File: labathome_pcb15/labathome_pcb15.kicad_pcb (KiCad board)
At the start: 2 copper layers, 100 x 100 mm, 244 parts, among them J1 HALL, J10 BMEx80, J11 QWIIC, J12 TCS34725, J13 POWER, J14 AUX OUT, J15 CAN RS 485, J16 Headphones, J17 Micro_SD_Card_Det1, J18 K1, J19 BH1750, J2 I2C, J20 CCS811, J21 GPIO, J22 Volts, J23 VL53L5x, J24 K1, J26 STDC14, J27 ADDA, J28 Brushless, J3 AUX IN, J30 Srv4, J31 Srv1, J32 Srv2, J33 Srv3, J34 STM32 EXT, J4 SCD4x, J5 USB_ESP32, J6 PROG, J7 FAN5V, J8 3V GN RGB 5V, J9 Barrel_Jack_Switch, K1 G6K-2, M1 W5500_mini, Q1 BC817, Q2 IRLML6344, Q3 TIP41, Q4 BC817, Q5 IRLML6344, SW1 Reset, SW2 ON RS TERM, SW3 ON CAN TERM, SW4 BATT POWER, SW5 POWER, SW6 YELLOW, SW7 RED, SW8 GREEN, SW9 PROG 5V POWER, U1 MAX3485, U10 NAU8822, U11 AMS1117, U12 AHT20, U13 DS18B20, U14 BMP280, U15 NRF24L01, U16 LM358, U17 DS18B20, U2 IP5306, U21 IPS_240_240, U22 AM612, U24 SRV05, U27 TPS54202DDC, U3 DRV8313, U4 ESP32-S3-WROOM-1, U5 STM32G431R8Tx, U6 RFM95W-868S2, U7 SN65HVD230, U8 SRV05-4, U9 LSM6DS3, X1 FAN_6024, X3 SIM7080G

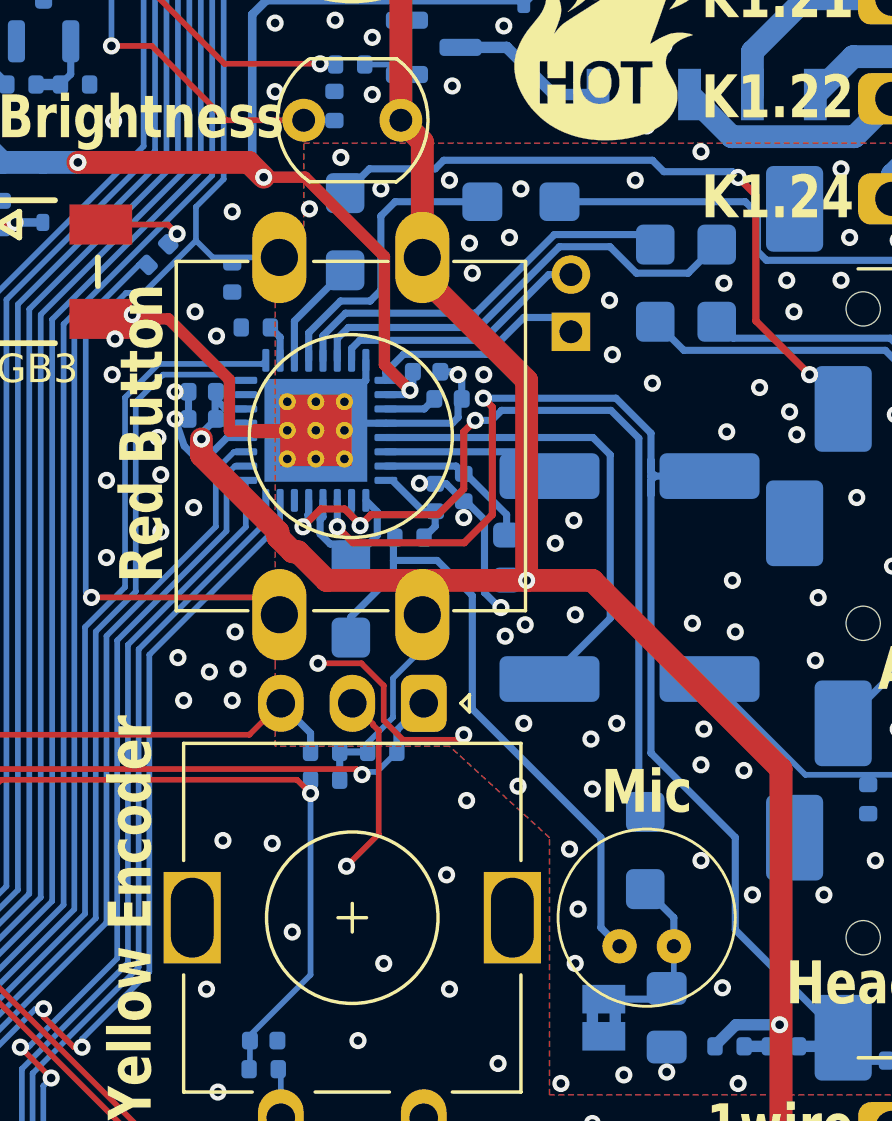
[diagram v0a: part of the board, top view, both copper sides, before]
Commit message: Added stm32 arduino firmware
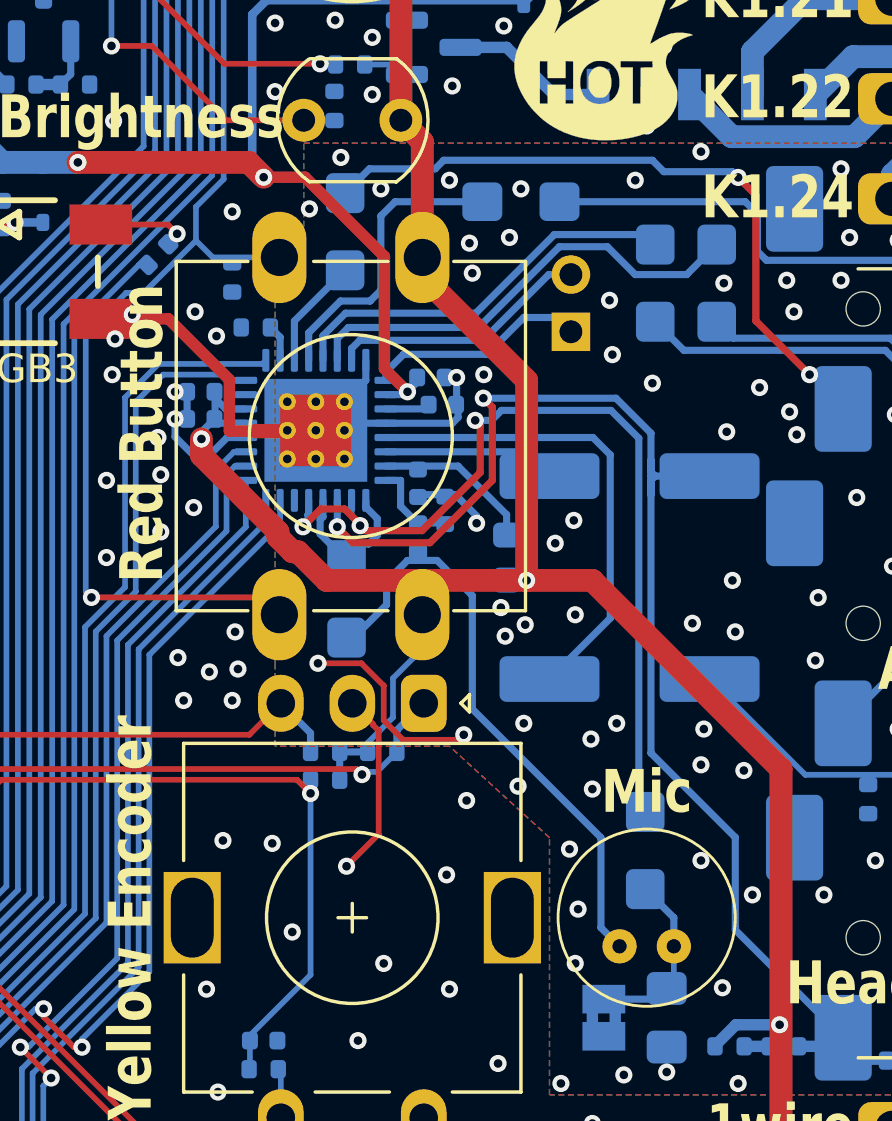
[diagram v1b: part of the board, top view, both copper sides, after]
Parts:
- moved C14 1.61 mm to (175.4, 99.1)
- moved C22 0.57 mm to (176.3, 100.0)
- moved R24 0.30 mm to (175.4, 101.0), turned to -90 degrees
- moved C21 0.28 mm to (176.2, 96.3)
- moved C15 0.25 mm to (175.8, 95.4)
- moved C23 0.15 mm to (172.9, 103.2)
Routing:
- net GNDA: track 22.1 -> 18.2 mm, vias 97 -> 96
- net Net-(MK1-+): track 21.7 -> 20.9 mm
- net /audioamplifier/JACK_DETECT: track 46.9 -> 46.2 mm

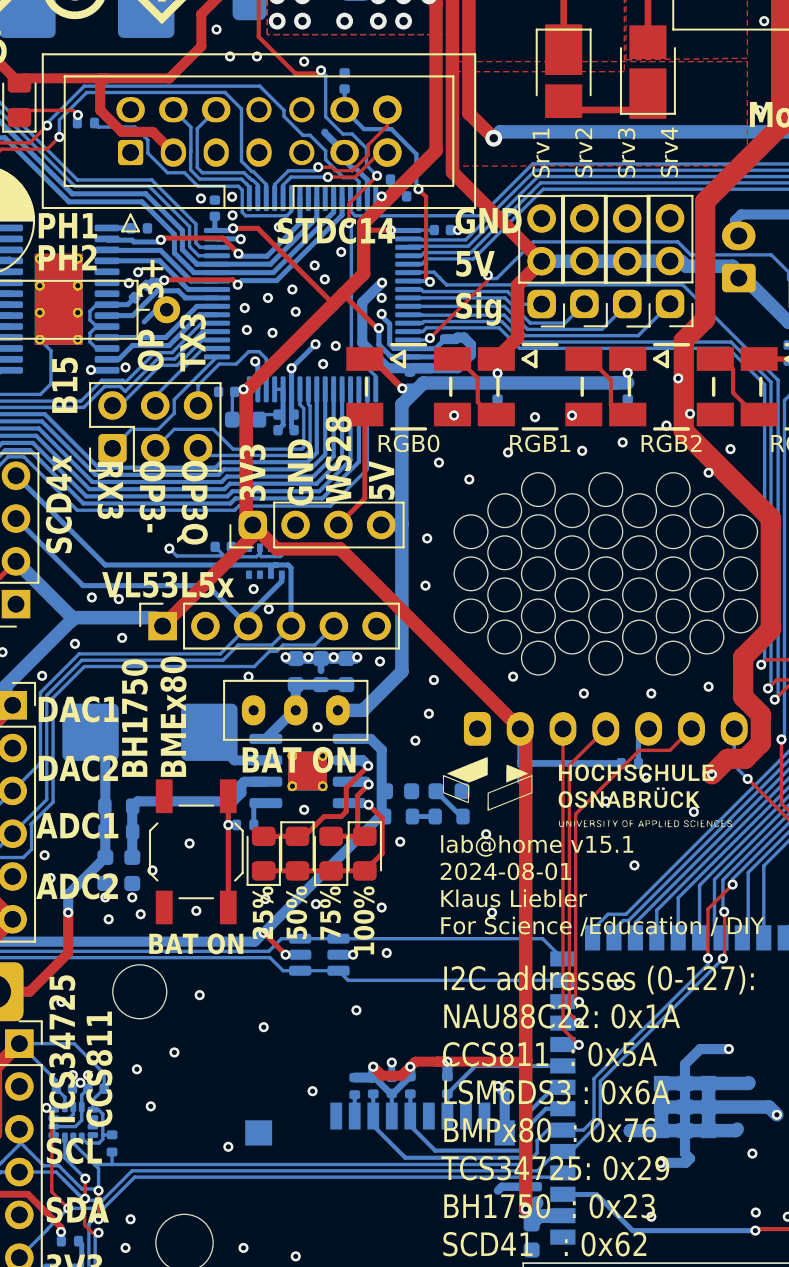
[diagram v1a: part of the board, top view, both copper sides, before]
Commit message: Updates in PCB, arduino test firmware
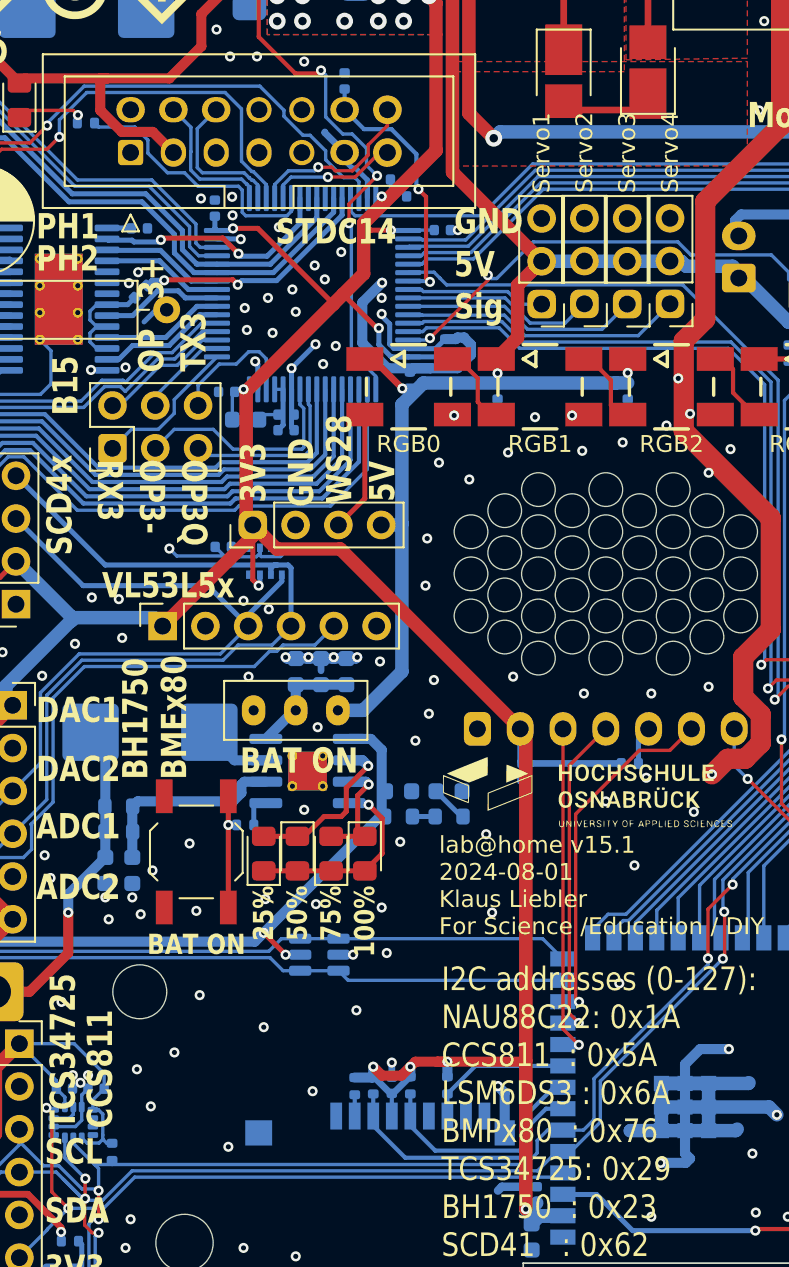
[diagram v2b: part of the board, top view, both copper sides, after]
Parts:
- J30: value Srv4 -> Servo4
- J31: value Srv1 -> Servo1
- J32: value Srv2 -> Servo2
- J33: value Srv3 -> Servo3
- U14: value BMP280 -> BMx280
- moved R44 0.50 mm to (120.7, 137.1)
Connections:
- U14 pad 2: unconnected-(U14-CSB-Pad2) -> +3V3
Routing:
- net +3V3: track 573.3 -> 577.8 mm, vias 62 -> 63
- net SCL: track 271.3 -> 270.8 mm

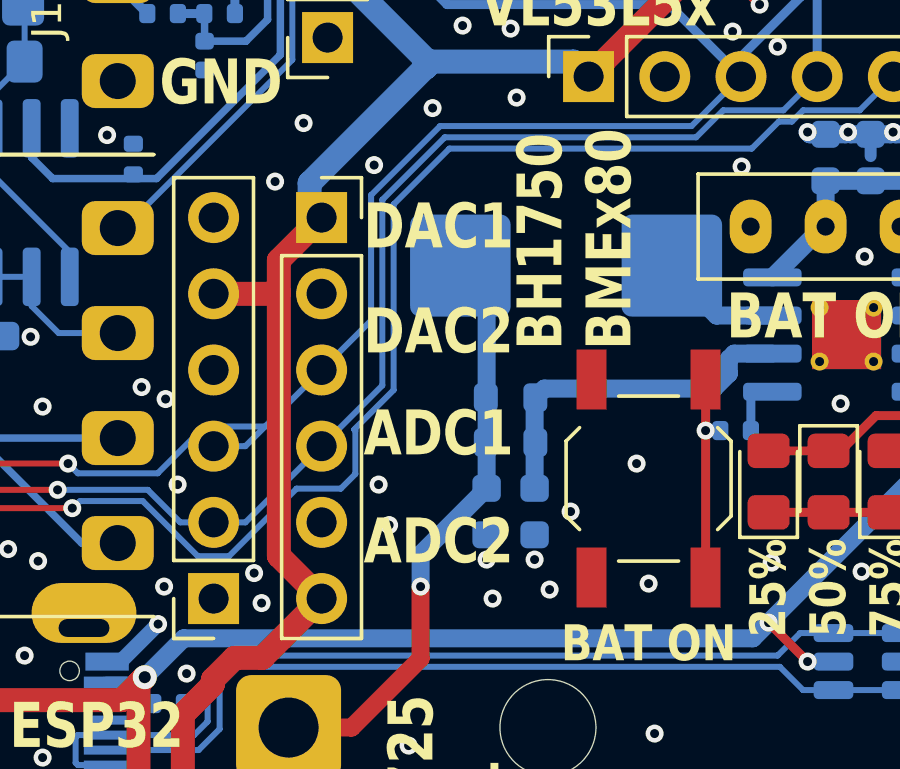
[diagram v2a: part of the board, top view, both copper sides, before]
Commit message: Re-enumerate Servos and Fans
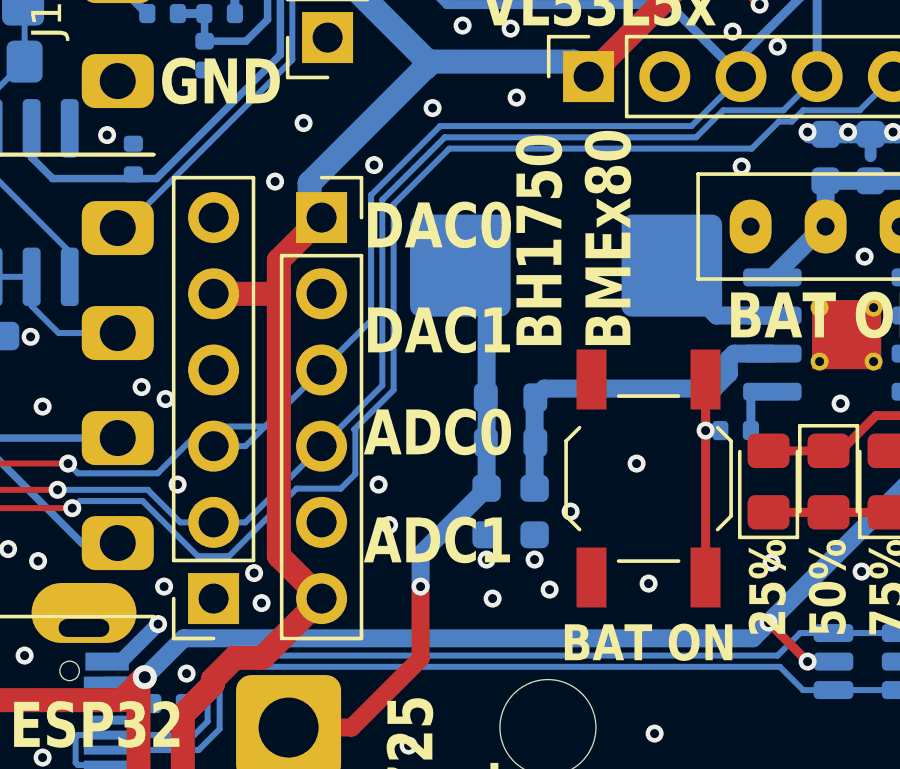
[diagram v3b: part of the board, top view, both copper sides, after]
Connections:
- net ADC_IN1 renamed ADC0
- net ADC_IN2 renamed ADC1
- net DAC1_OUT1 renamed DAC0
- net DAC1_OUT2 renamed DAC1
- net DAC1_OUT2x renamed DAC1x
- net FAN2_DRIVE renamed FAN_DRIVE
- J30 pad 1: Servo4 -> Servo3
- J31 pad 1: Servo1 -> Servo0
- J32 pad 1: Servo2 -> Servo1
- J33 pad 1: Servo3 -> Servo2
- U5 pad 10: Servo3 -> Servo2
- U5 pad 11: Servo4 -> Servo3
- U5 pad 8: Servo1 -> Servo0
- U5 pad 9: Servo2 -> Servo1
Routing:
- net Servo4: track 16.8 -> 0.00 mm
- net Servo0: track 0.00 -> 8.28 mm
- net Servo1: track 8.28 -> 11.5 mm
- net Servo3: track 14.2 -> 16.8 mm
- net Servo2: track 11.5 -> 14.2 mm
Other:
- board text added: "ADC0"
- board text added: "DAC0"
- board text removed: "ADC2"
- board text removed: "DAC2"
